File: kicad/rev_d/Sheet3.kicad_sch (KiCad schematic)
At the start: 106 parts, among them U1 74HCT1G04, X10 ST-214C, X14 AAFP/AC97 audio, X16 PLB1-4I, X17 PLB1-4I, X18 PLB1-4I, X20 PLB1-4I

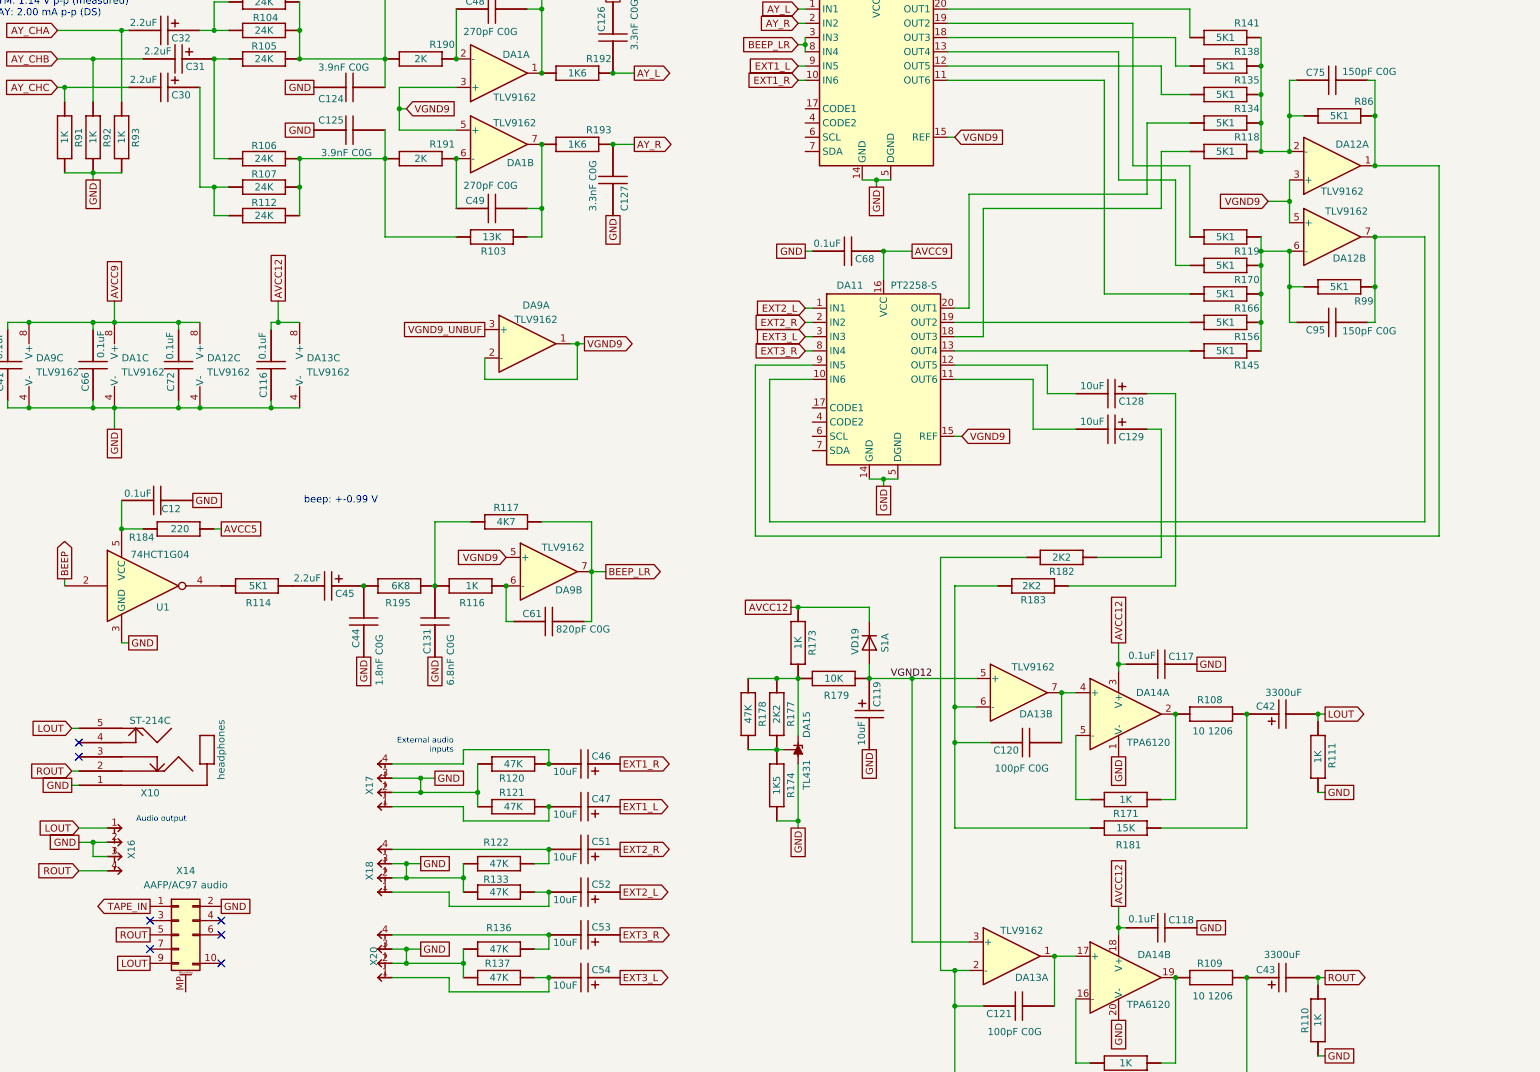
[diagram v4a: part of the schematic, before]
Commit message: pentevo: rev D: add connection of pt2258 to I2C, add extra gnd pin to AAFP/AC97 connector
git-svn-id: svn://localhost/local-pentevo@1257 c6c76956-fad2-4150-a3a9-ea0a427205ba
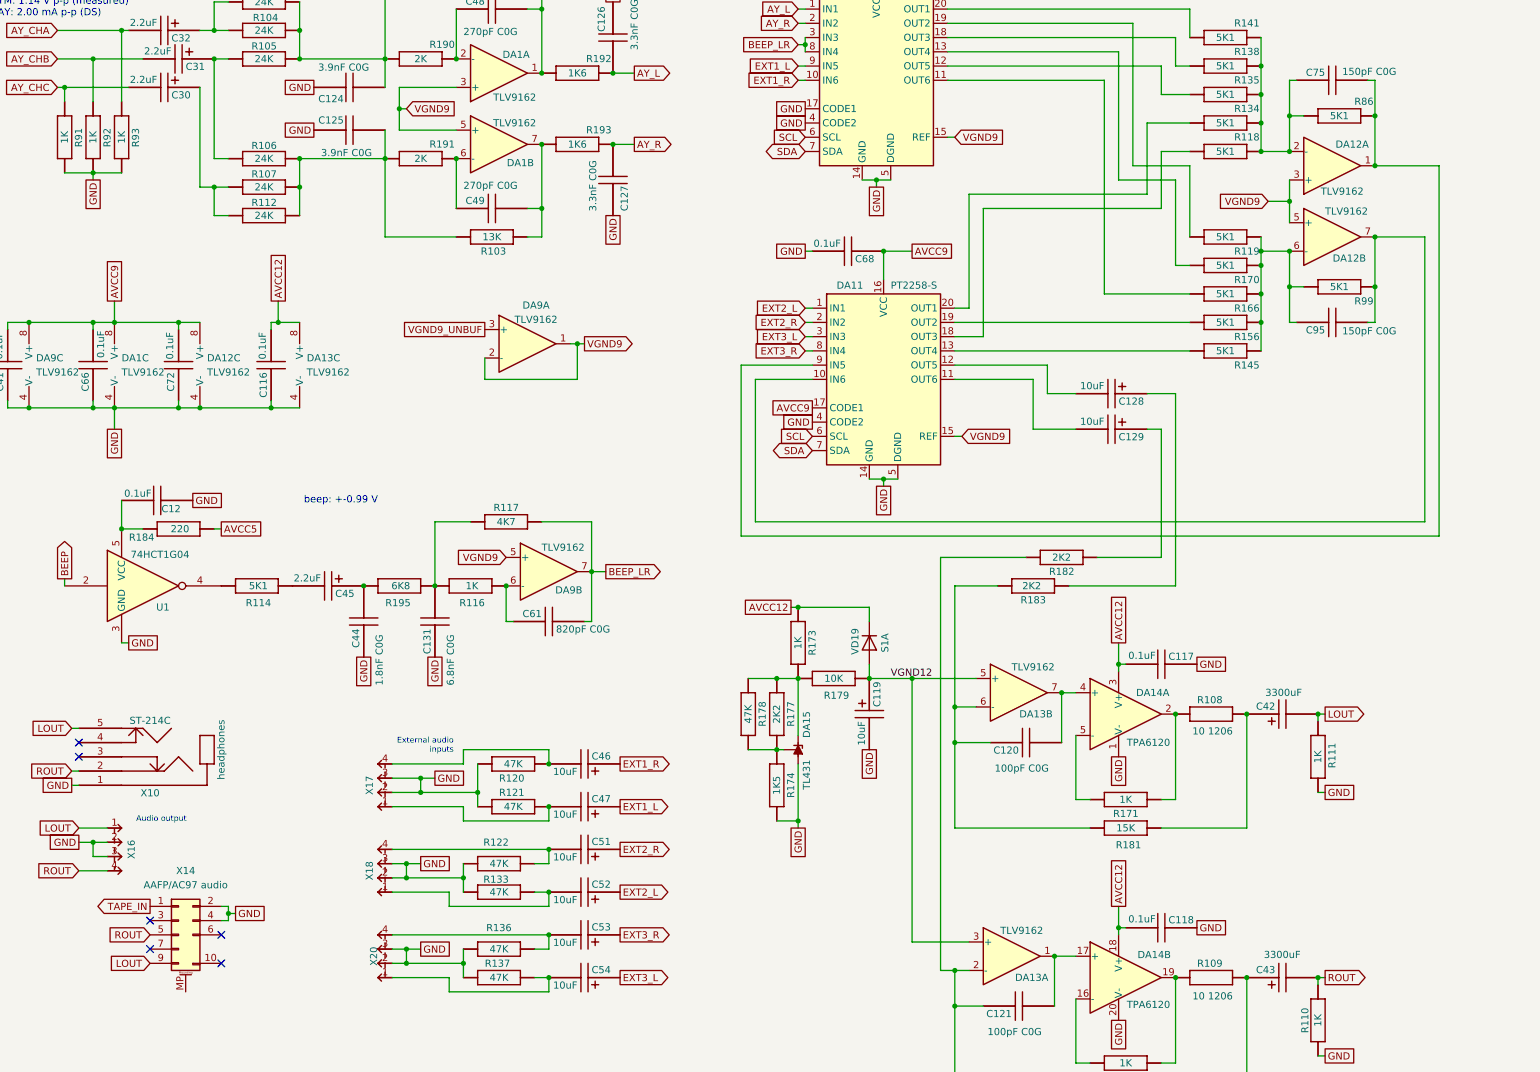
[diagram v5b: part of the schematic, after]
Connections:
- net AVCC9: now also DA11.17 (CODE1)
- net GND: now also DA10.17 (CODE1), DA10.4 (CODE2), DA11.4 (CODE2), X14.4 (Pin_4)
- net SCL: now reaches DA11.6 (SCL)
- net SCL: now also DA10.6 (SCL)
- net SDA: now reaches DA11.7 (SDA)
- net SDA: now also DA10.7 (SDA)
- no-connect marks 7 -> 6
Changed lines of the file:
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@@
 	)
 	(junction
+		(at 68.58 208.28)
+		(diameter 0)
+		(color 0 0 0 0)
+	)
+	(junction
 		(at 171.45 53.34)
 		(diameter 0)
@@
 	)
 	(no_connect
-		(at 67.31 209.55)
-	)
-	(no_connect
 		(at 41.91 177.8)
 	)
@@
 	(wire
 		(pts
+			(xy 68.58 207.01) (xy 67.31 207.01)
+		)
+		(stroke
+			(width 0)
+			(type default)
+		)
+	)
+	(wire
+		(pts
 			(xy 198.12 113.03) (xy 212.09 113.03)
 		)
@@
 		)
 	)
+	(wire
+		(pts
+			(xy 69.85 208.28) (xy 68.58 208.28)
+		)
+		(stroke
+			(width 0)
+			(type default)
+		)
+	)
 	(polyline
 		(pts
@@
 	(wire
 		(pts
+			(xy 68.58 208.28) (xy 68.58 207.01)
+		)
+		(stroke
+			(width 0)
+			(type default)
+		)
+	)
+	(wire
+		(pts
 			(xy 240.03 97.79) (xy 224.79 97.79)
 		)
@@
 	(wire
 		(pts
-			(xy 165.1 138.43) (xy 165.1 113.03)
+			(xy 162.56 138.43) (xy 162.56 113.03)
 		)
 		(stroke
@@
 	(wire
 		(pts
+			(xy 68.58 208.28) (xy 68.58 209.55)
+		)
+		(stroke
+			(width 0)
+			(type default)
+		)
+	)
+	(wire
+		(pts
 			(xy 237.49 57.15) (xy 240.03 57.15)
 		)
@@
 	(wire
 		(pts
-			(xy 162.56 140.97) (xy 162.56 110.49)
+			(xy 160.02 140.97) (xy 160.02 110.49)
 		)
 		(stroke
@@
 	(wire
 		(pts
-			(xy 284.48 140.97) (xy 162.56 140.97)
+			(xy 284.48 140.97) (xy 160.02 140.97)
 		)
 		(stroke
@@
 	(wire
 		(pts
-			(xy 162.56 110.49) (xy 172.72 110.49)
+			(xy 160.02 110.49) (xy 172.72 110.49)
 		)
 		(stroke
@@
 	(wire
 		(pts
+			(xy 68.58 209.55) (xy 67.31 209.55)
+		)
+		(stroke
+			(width 0)
+			(type default)
+		)
+	)
+	(wire
+		(pts
 			(xy 125.73 219.71) (xy 125.73 222.25)
 		)
@@
 	(wire
 		(pts
-			(xy 165.1 113.03) (xy 172.72 113.03)
+			(xy 162.56 113.03) (xy 172.72 113.03)
 		)
 		(stroke
@@
 	(wire
 		(pts
-			(xy 281.94 138.43) (xy 165.1 138.43)
+			(xy 281.94 138.43) (xy 162.56 138.43)
 		)
 		(stroke
@@
 		)
 	)
+	(global_label "SDA"
+		(shape bidirectional)
+		(at 172.72 125.73 180)
+		(fields_autoplaced yes)
+		(effects
+			(font
+				(size 1.27 1.27)
+			)
+			(justify right)
+		)
+		(property "Intersheetrefs" "${INTERSHEET_REFS}"
+			(at 165.0554 125.73 0)
+			(effects
+				(font
+					(size 1.27 1.27)
+				)
+				(justify right)
+				(hide yes)
+			)
+		)
+	)
 	(global_label "GND"
 		(shape passive)
@@
 	)
 	(global_label "ROUT"
-		(shape passive)
+		(shape input)
 		(at 54.61 212.09 180)
 		(fields_autoplaced yes)
@@
 		)
 		(property "Intersheetrefs" "${INTERSHEET_REFS}"
-			(at 47.8375 212.09 0)
+			(at 46.7262 212.09 0)
 			(effects
 				(font
@@
 	(global_label "GND"
 		(shape passive)
+		(at 171.45 67.31 180)
+		(fields_autoplaced yes)
+		(effects
+			(font
+				(size 1.27 1.27)
+			)
+			(justify right)
+		)
+		(property "Intersheetrefs" "${INTERSHEET_REFS}"
+			(at 165.7056 67.31 0)
+			(effects
+				(font
+					(size 1.27 1.27)
+				)
+				(justify right)
+				(hide yes)
+			)
+		)
+	)
+	(global_label "GND"
+		(shape passive)
 		(at 40.64 185.42 180)
 		(fields_autoplaced yes)
@@
 		)
 	)
+	(global_label "GND"
+		(shape passive)
+		(at 172.72 120.65 180)
+		(fields_autoplaced yes)
+		(effects
+			(font
+				(size 1.27 1.27)
+			)
+			(justify right)
+		)
+		(property "Intersheetrefs" "${INTERSHEET_REFS}"
+			(at 166.9756 120.65 0)
+			(effects
+				(font
+					(size 1.27 1.27)
+				)
+				(justify right)
+				(hide yes)
+			)
+		)
+	)
 	(global_label "EXT3_L"
 		(shape input)
@@
 		)
 	)
+	(global_label "SCL"
+		(shape input)
+		(at 171.45 69.85 180)
+		(fields_autoplaced yes)
+		(effects
+			(font
+				(size 1.27 1.27)
+			)
+			(justify right)
+		)
+		(property "Intersheetrefs" "${INTERSHEET_REFS}"
+			(at 164.9572 69.85 0)
+			(effects
+				(font
+					(size 1.27 1.27)
+				)
+				(justify right)
+				(hide yes)
+			)
+		)
+	)
 	(global_label "LOUT"
 		(shape output)
@@
 		)
 	)
+	(global_label "AVCC9"
+		(shape passive)
+		(at 172.72 118.11 180)
+		(fields_autoplaced yes)
+		(effects
+			(font
+				(size 1.27 1.27)
+			)
+			(justify right)
+		)
+		(property "Intersheetrefs" "${INTERSHEET_REFS}"
+			(at 164.9194 118.11 0)
+			(effects
+				(font
+					(size 1.27 1.27)
+				)
+				(justify right)
+				(hide yes)
+			)
+		)
+	)
 	(global_label "AY_R"
 		(shape input)
@@
 		)
 	)
+	(global_label "SDA"
+		(shape bidirectional)
+		(at 171.45 72.39 180)
+		(fields_autoplaced yes)
+		(effects
+			(font
+				(size 1.27 1.27)
+			)
+			(justify right)
+		)
+		(property "Intersheetrefs" "${INTERSHEET_REFS}"
+			(at 163.7854 72.39 0)
+			(effects
+				(font
+					(size 1.27 1.27)
+				)
+				(justify right)
+				(hide yes)
+			)
+		)
+	)
 	(global_label "ROUT"
 		(shape input)
@@
 	(global_label "GND"
 		(shape passive)
+		(at 171.45 64.77 180)
+		(fields_autoplaced yes)
+		(effects
+			(font
+				(size 1.27 1.27)
+			)
+			(justify right)
+		)
+		(property "Intersheetrefs" "${INTERSHEET_REFS}"
+			(at 165.7056 64.77 0)
+			(effects
+				(font
+					(size 1.27 1.27)
+				)
+				(justify right)
+				(hide yes)
+			)
+		)
+	)
+	(global_label "GND"
+		(shape passive)
 		(at 62.23 134.62 0)
 		(fields_autoplaced yes)
@@
 		)
 	)
+	(global_label "SCL"
+		(shape input)
+		(at 172.72 123.19 180)
+		(fields_autoplaced yes)
+		(effects
+			(font
+				(size 1.27 1.27)
+			)
+			(justify right)
+		)
+		(property "Intersheetrefs" "${INTERSHEET_REFS}"
+			(at 166.2272 123.19 0)
+			(effects
+				(font
+					(size 1.27 1.27)
+				)
+				(justify right)
+				(hide yes)
+			)
+		)
+	)
 	(global_label "GND"
 		(shape passive)
@@
 	(global_label "GND"
 		(shape passive)
-		(at 67.31 207.01 0)
+		(at 69.85 208.28 0)
 		(fields_autoplaced yes)
 		(effects
@@
 		)
 		(property "Intersheetrefs" "${INTERSHEET_REFS}"
-			(at 73.0544 207.01 0)
+			(at 75.5944 208.28 0)
 			(effects
 				(font
@@
 	)
 	(global_label "LOUT"
-		(shape passive)
+		(shape input)
 		(at 54.61 217.17 180)
 		(fields_autoplaced yes)
@@
 		)
 		(property "Intersheetrefs" "${INTERSHEET_REFS}"
-			(at 48.0794 217.17 0)
+			(at 46.9681 217.17 0)
 			(effects
 				(font

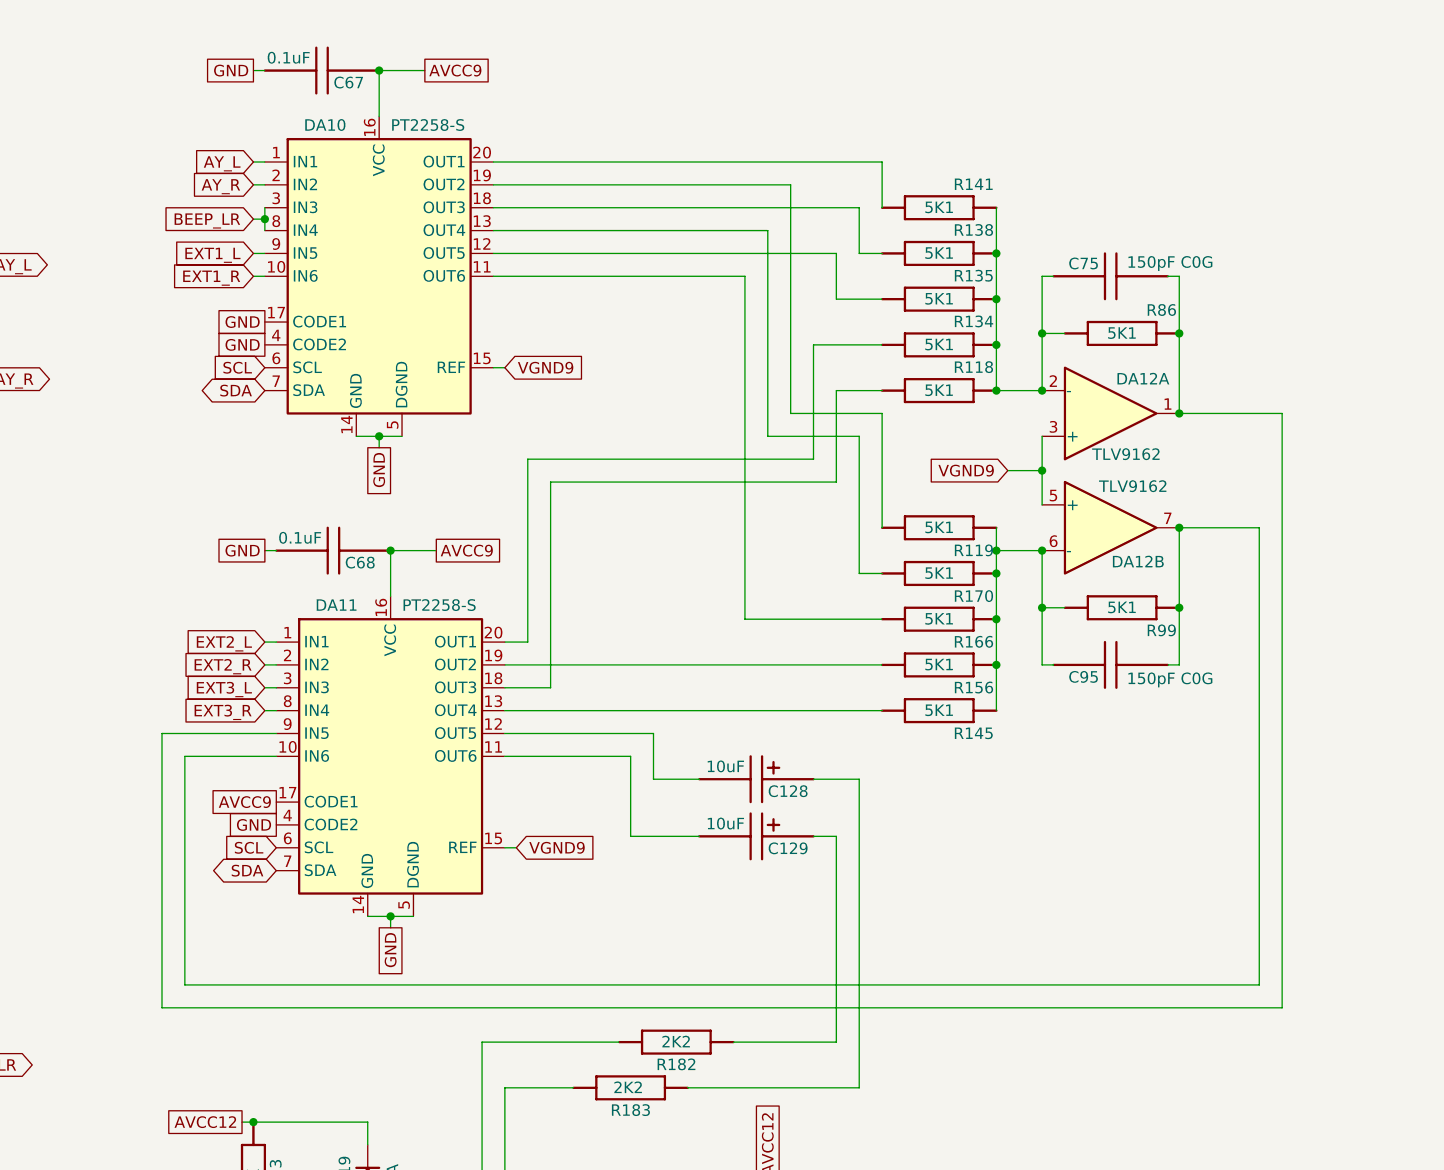
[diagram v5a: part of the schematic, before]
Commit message: pentevo: rev D: beautify audio schematics page, change vcc_mega to vcc5 convertor for high ROM addrs
git-svn-id: svn://localhost/local-pentevo@1258 c6c76956-fad2-4150-a3a9-ea0a427205ba
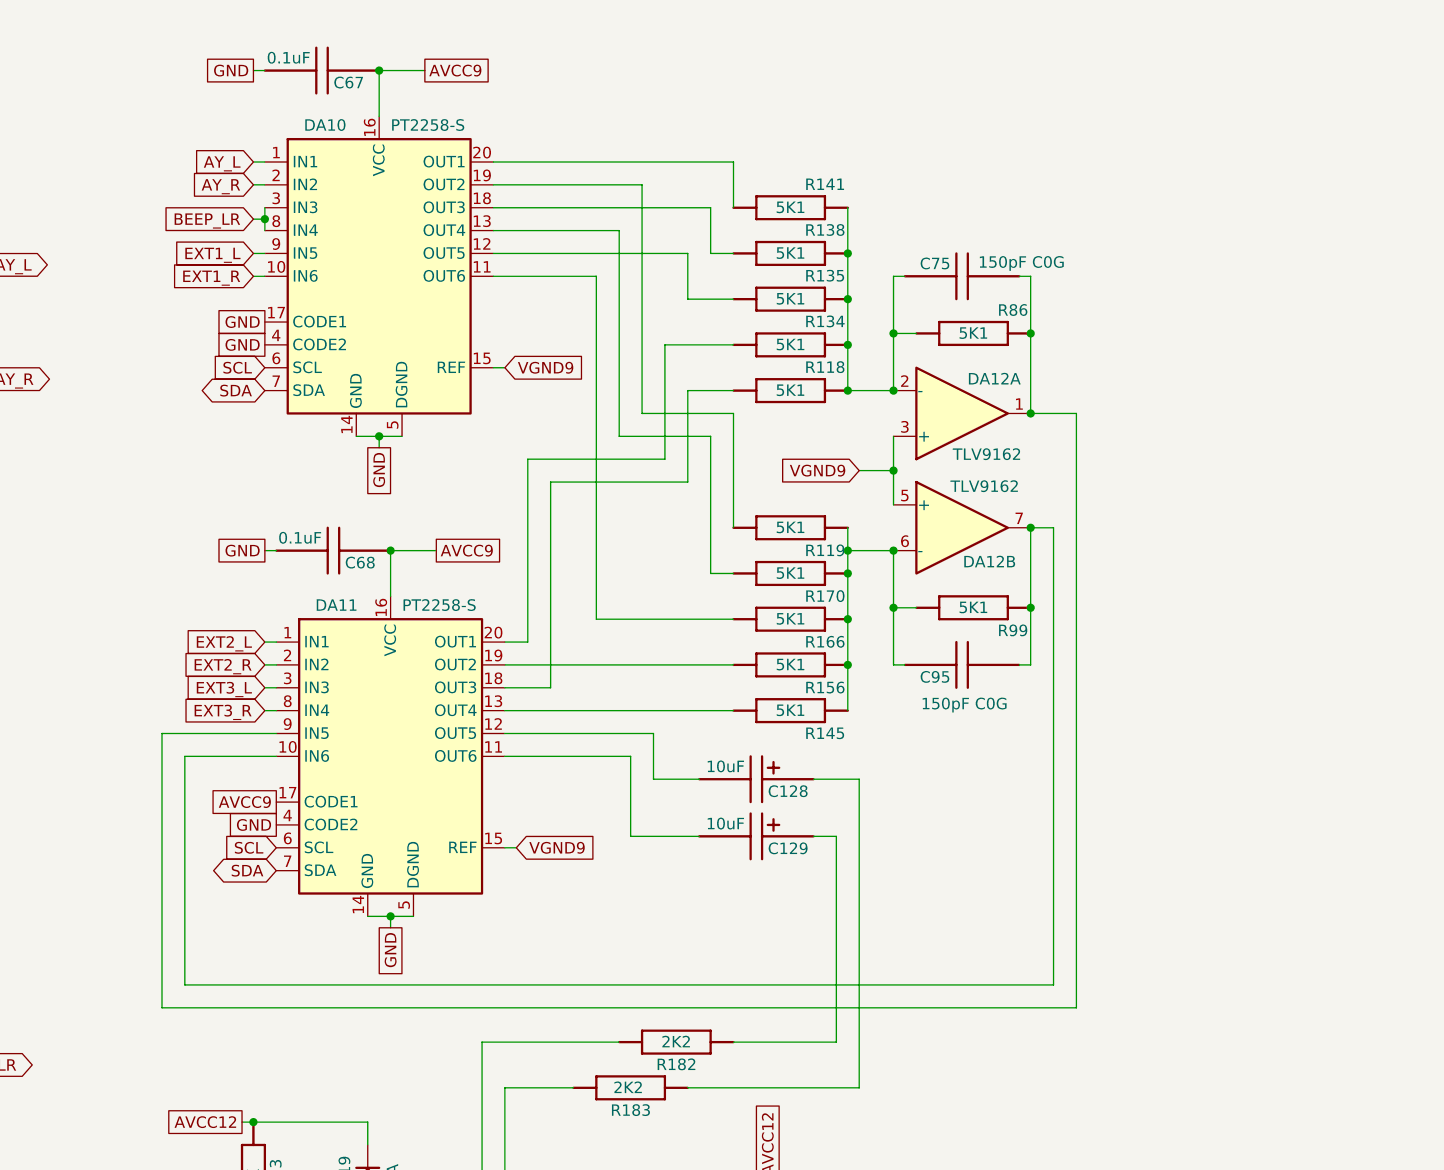
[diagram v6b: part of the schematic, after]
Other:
- moved on the sheet: C75, C95, DA12A, DA12B, R118, R119, R134, R135, R138, R141, R145, R156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
